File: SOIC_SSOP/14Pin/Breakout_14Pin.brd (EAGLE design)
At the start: 14.2 x 18.1 mm, 4 parts, among them U1 GEN_14SOIC, U2 GEN_14TSSOP

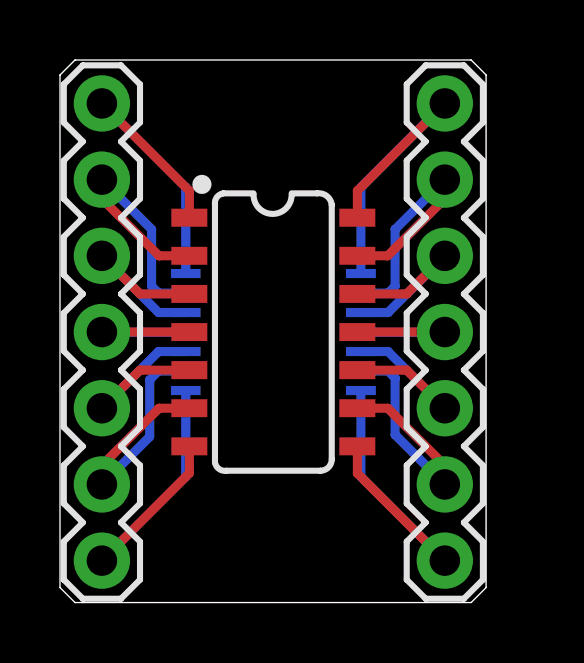
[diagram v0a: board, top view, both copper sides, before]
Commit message: Fixed spacing on SOIC/SSOP 14 breakout
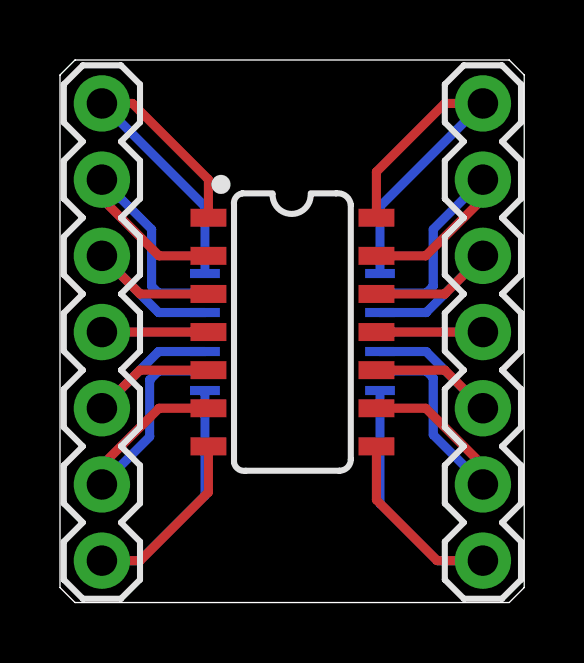
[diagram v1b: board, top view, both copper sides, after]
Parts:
- moved J2 1.27 mm to (14.1, 16.6)
- moved U1 0.63 mm to (7.75, 9.65)
- moved U2 0.63 mm to (7.75, 9.02)
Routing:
- net 8: track 11.8 -> 14.2 mm
- net 7: track 11.8 -> 13.9 mm
- net 9: track 9.81 -> 11.1 mm
- net 10: track 7.02 -> 8.29 mm
- net 6: track 9.81 -> 11.1 mm
- net 5: track 7.02 -> 8.29 mm
- net 4: track 5.71 -> 6.98 mm
- net 3: track 7.02 -> 8.29 mm
- net 2: track 9.81 -> 11.1 mm
- net 13: track 9.81 -> 11.1 mm
- net 12: track 7.02 -> 8.29 mm
- net 11: track 5.71 -> 6.98 mm
- net 14: track 11.8 -> 13.1 mm
- net 1: track 11.8 -> 13.0 mm
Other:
- board size 14.2 x 18.1 mm -> 15.5 x 18.1 mm
